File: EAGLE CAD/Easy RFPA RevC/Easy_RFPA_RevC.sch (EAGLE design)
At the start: 295 parts, among them IC1 LM741D, IC2 LM741D, IC3 LM393D, IC5 74AHC1G00DBV, IC6 74LS74D, IC7 74AHC1G86DBV, J401 HDR_2X1282836-1282836-1, J402 KK_PCFAN, Q1 IRF630, Q101 IRF520N, Q102 IRF630, Q2 MOSFET_NBSS123SOT23, Q201 IRF630, Q202 IRF630, Q3 NPNMMBT3904SOT23_BEC, Q301 MOSFET_NBSS123SOT23, Q302 PNPSOT23_BEC, Q303 NPNMMBT3904SOT23_BEC, Q4 PNPSOT23_BEC, Q5 IRF630, SW1 SPST_NO_TACT_RA43125608371643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, SW2 SPST_NO_TACT_RA43125608371643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, T1 HP1_TRAFO, T102 HP4_TRAFO, U1 OPAMP_QUADTLV274IDSOIC14, U2 ADJ_ZENERTL431AILPRAGTO-92-LP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, U302 OPAMP_QUADTLV274IDSOIC14, U401 LDO_3TERMMC78M12CTGTO220_VERT, U402 LDO_3TERMMC78M05CTGTO220_VERT, X1 1-227161-0, X2 1-227161-0, X4 1-227161-0, X402 HEATSINK_OMNI_DUALOMNI-UNI-30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

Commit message: Put discrete LDO on board
Remove old zeners
Move smaller electrolytic caps towards load circuitry to free up space
Move extra mounting holes onto board
Should consider reordering buttons/LEDs on west edge
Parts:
- removed D402, D5: D-ZENER1N5355B-TPDO15-12, MDT_Diode:D-ZENER1N5355B-TPDO15-12
- removed R402, R403: 1.0, MDT_R:R90GENR1206
- added C31: 22uF, MDT_C:CPOLC-22U-63V-20%-6.3DX12.5L-ELECE2,5-7
- added X6, X7: HEATSINK_CLIPONATS-PCBT1085ATS-PCBT1085, MDT_HEATSINK:HEATSINK_CLIPONATS-PCBT1085ATS-PCBT1085
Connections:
- removed net N$28: D5.A1, R403.1
- removed net N$32: D402.A1, R402.1
- net +24V: now also C31.+; no longer R402.2, R403.2
- net GND: now also C31.-
- net VB_ICL: no longer D402.C1, D5.C1
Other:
- moved on the sheet: C30, C401, D401, F401, H1, H2, H401, H402, H403, H404, J401, Q5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

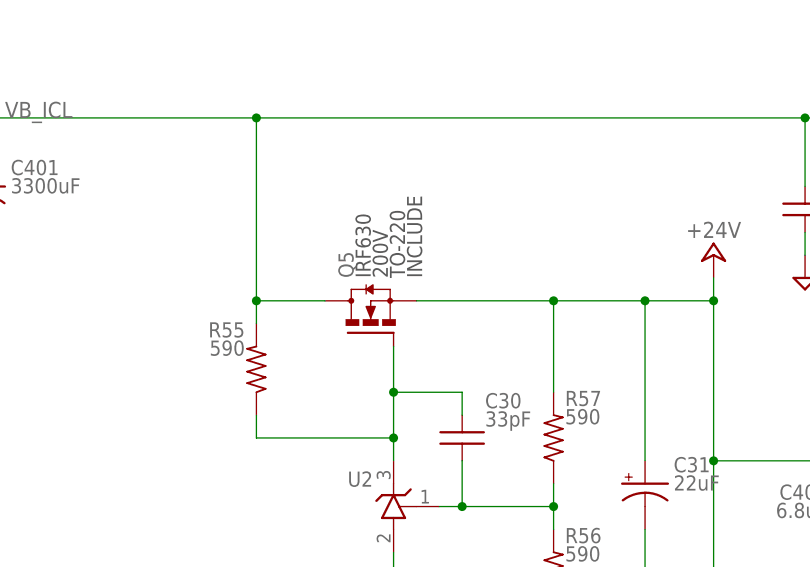
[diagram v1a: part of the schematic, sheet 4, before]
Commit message: TIP122 and angle bracket
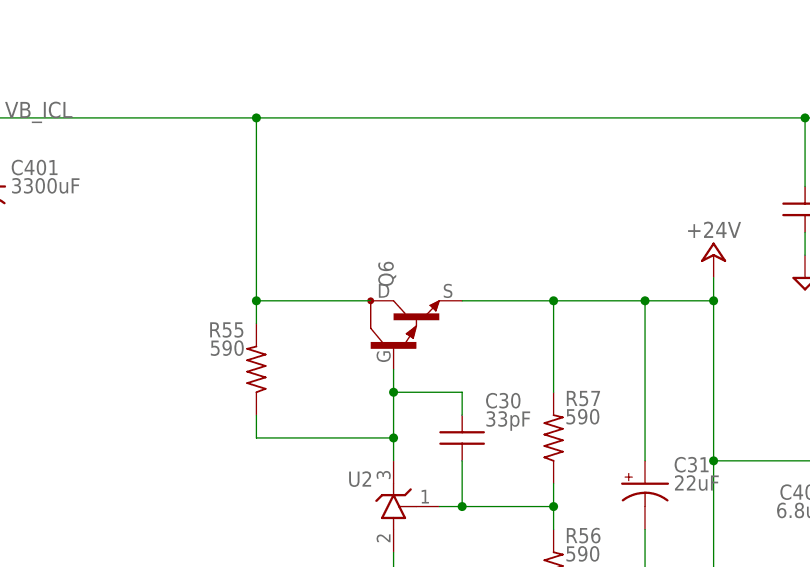
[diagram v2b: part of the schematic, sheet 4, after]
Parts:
- removed Q5: IRF630, MDT_TRANS:MOSFET_NIRF630TO-220-VERT
- added Q6: NPN_DARGLINGTONTIP122TO220BV, MDT_TRANS:NPN_DARGLINGTONTIP122TO220BV
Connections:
- net +24V: now also Q6.E; no longer Q5.S
- net N$92: now also Q6.B; no longer Q5.G
- net VB_ICL: now also Q6.C; no longer Q5.D
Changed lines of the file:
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@@
 </part>
 <part name="SUPPLY52" library="supply2" deviceset="GND" device=""/>
-<part name="Q5" library="MDT_TRANS" deviceset="MOSFET_N" device="TO-220-VERT" technology="IRF630" value="IRF630">
-<variant name="IRF520N_20W" populate="no"/>
-</part>
 <part name="U2" library="MDT_VREF" deviceset="ADJ_ZENER" device="TO-92-LPRE" technology="TL431AILPRAG"/>
 <part name="R56" library="MDT_R" deviceset="R" device="0805_IPC" technology="GEN" value="590"/>
@@
 <part name="C31" library="MDT_C" deviceset="CPOL" device="E2,5-7" technology="C-22U-63V-20%-6.3DX12.5L-ELEC" value="22uF"/>
 <part name="SUPPLY55" library="supply2" deviceset="GND" device=""/>
+<part name="Q6" library="MDT_TRANS" deviceset="NPN_DARGLINGTON" device="TO220BV" technology="TIP122"/>
 </parts>
 <sheets>
@@
 <instance part="X3" gate="G$1" x="350.52" y="78.74"/>
 <instance part="X5" gate="G$1" x="365.76" y="73.66"/>
-<instance part="Q5" gate="G$1" x="132.08" y="154.94" rot="R90"/>
 <instance part="U2" gate="G$1" x="134.62" y="132.08" rot="MR0"/>
 <instance part="R56" gate="G$1" x="152.4" y="124.46"/>
@@
 <instance part="C31" gate="G$1" x="162.56" y="134.62"/>
 <instance part="SUPPLY55" gate="GND" x="162.56" y="116.84" smashed="yes"/>
+<instance part="Q6" gate="G$1" x="134.62" y="152.4" rot="R90"/>
 </instances>
 <busses>
@@
 <segment>
 <wire x1="119.38" y1="152.4" x2="119.38" y2="154.94" width="0.1524" layer="91"/>
-<pinref part="Q5" gate="G$1" pin="D"/>
-<wire x1="119.38" y1="154.94" x2="127" y2="154.94" width="0.1524" layer="91"/>
+<wire x1="119.38" y1="154.94" x2="132.08" y2="154.94" width="0.1524" layer="91"/>
 <pinref part="R55" gate="G$1" pin="1"/>
 <pinref part="R401" gate="G$1" pin="2"/>
@@
 <junction x="119.38" y="154.94"/>
 <junction x="119.38" y="175.26"/>
+<pinref part="Q6" gate="G$1" pin="C"/>
 </segment>
 </net>
@@
 <pinref part="U2" gate="G$1" pin="C"/>
 <wire x1="134.62" y1="144.78" x2="134.62" y2="139.7" width="0.1524" layer="91"/>
-<pinref part="Q5" gate="G$1" pin="G"/>
 <wire x1="134.62" y1="139.7" x2="134.62" y2="137.16" width="0.1524" layer="91"/>
-<wire x1="134.62" y1="149.86" x2="134.62" y2="144.78" width="0.1524" layer="91"/>
-<junction x="134.62" y="144.78"/>
 <wire x1="119.38" y1="139.7" x2="134.62" y2="139.7" width="0.1524" layer="91"/>
 <junction x="134.62" y="139.7"/>
 <pinref part="R55" gate="G$1" pin="2"/>
+<pinref part="Q6" gate="G$1" pin="B"/>
+<wire x1="134.62" y1="144.78" x2="134.62" y2="147.32" width="0.1524" layer="91"/>
+<junction x="134.62" y="144.78"/>
 </segment>
 </net>
@@
 <wire x1="170.18" y1="157.48" x2="170.18" y2="154.94" width="0.1524" layer="91"/>
 <junction x="170.18" y="137.16"/>
-<pinref part="Q5" gate="G$1" pin="S"/>
 <pinref part="R57" gate="G$1" pin="1"/>
 <wire x1="170.18" y1="154.94" x2="170.18" y2="137.16" width="0.1524" layer="91"/>
-<wire x1="137.16" y1="154.94" x2="152.4" y2="154.94" width="0.1524" layer="91"/>
+<wire x1="142.24" y1="154.94" x2="152.4" y2="154.94" width="0.1524" layer="91"/>
 <wire x1="152.4" y1="154.94" x2="152.4" y2="144.78" width="0.1524" layer="91"/>
 <wire x1="152.4" y1="154.94" x2="162.56" y2="154.94" width="0.1524" layer="91"/>
@@
 <wire x1="162.56" y1="137.16" x2="162.56" y2="154.94" width="0.1524" layer="91"/>
 <junction x="162.56" y="154.94"/>
-</segment>
-</net>
+<pinref part="Q6" gate="G$1" pin="E"/>
+</segment>
+</net>
